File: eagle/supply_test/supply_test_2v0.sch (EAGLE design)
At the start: 27 parts, among them J21 AC_INSW, Q1 2N7002, U1 TPS62122

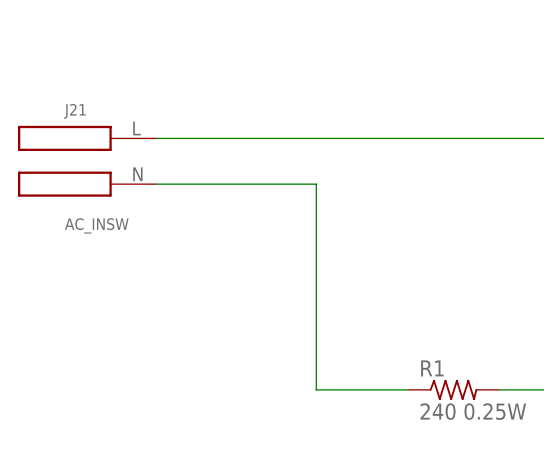
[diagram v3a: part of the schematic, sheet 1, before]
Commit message: finished updating shcematic
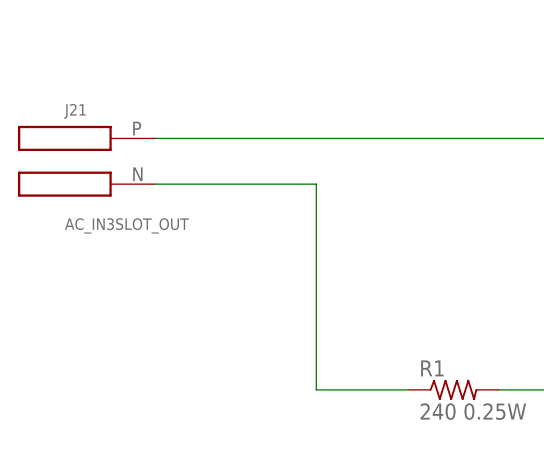
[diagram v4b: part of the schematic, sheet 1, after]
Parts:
- J21: value AC_INSW -> AC_IN3SLOT_OUT; device powerfilm:AC_INSW -> powerfilm:AC_IN3SLOT_OUT
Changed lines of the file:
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@@
 <grid distance="0.1" unitdist="inch" unit="inch" style="lines" multiple="1" display="no" altdistance="0.01" altunitdist="inch" altunit="inch"/>
 <layers>
-<layer number="1" name="Top" color="4" fill="1" visible="no" active="no"/>
-<layer number="2" name="Route2" color="1" fill="3" visible="no" active="no"/>
-<layer number="3" name="Route3" color="4" fill="3" visible="no" active="no"/>
-<layer number="4" name="Route4" color="1" fill="4" visible="no" active="no"/>
-<layer number="5" name="Route5" color="4" fill="4" visible="no" active="no"/>
-<layer number="6" name="Route6" color="1" fill="8" visible="no" active="no"/>
-<layer number="7" name="Route7" color="4" fill="8" visible="no" active="no"/>
-<layer number="8" name="Route8" color="1" fill="2" visible="no" active="no"/>
-<layer number="9" name="Route9" color="4" fill="2" visible="no" active="no"/>
-<layer number="10" name="Route10" color="1" fill="7" visible="no" active="no"/>
-<layer number="11" name="Route11" color="4" fill="7" visible="no" active="no"/>
-<layer number="12" name="Route12" color="1" fill="5" visible="no" active="no"/>
-<layer number="13" name="Route13" color="4" fill="5" visible="no" active="no"/>
-<layer number="14" name="Route14" color="1" fill="6" visible="no" active="no"/>
-<layer number="15" name="Route15" color="4" fill="6" visible="no" active="no"/>
-<layer number="16" name="Bottom" color="1" fill="1" visible="no" active="no"/>
-<layer number="17" name="Pads" color="2" fill="1" visible="no" active="no"/>
-<layer number="18" name="Vias" color="2" fill="1" visible="no" active="no"/>
-<layer number="19" name="Unrouted" color="6" fill="1" visible="no" active="no"/>
-<layer number="20" name="Dimension" color="15" fill="1" visible="no" active="no"/>
-<layer number="21" name="tPlace" color="7" fill="1" visible="no" active="no"/>
-<layer number="22" name="bPlace" color="7" fill="1" visible="no" active="no"/>
-<layer number="23" name="tOrigins" color="15" fill="1" visible="no" active="no"/>
-<layer number="24" name="bOrigins" color="15" fill="1" visible="no" active="no"/>
-<layer number="25" name="tNames" color="7" fill="1" visible="no" active="no"/>
-<layer number="26" name="bNames" color="7" fill="1" visible="no" active="no"/>
-<layer number="27" name="tValues" color="7" fill="1" visible="no" active="no"/>
-<layer number="28" name="bValues" color="7" fill="1" visible="no" active="no"/>
+<layer number="1" name="Top" color="4" fill="1" visible="yes" active="no"/>
+<layer number="2" name="Route2" color="1" fill="3" visible="yes" active="no"/>
+<layer number="3" name="Route3" color="4" fill="3" visible="yes" active="no"/>
+<layer number="4" name="Route4" color="1" fill="4" visible="yes" active="no"/>
+<layer number="5" name="Route5" color="4" fill="4" visible="yes" active="no"/>
+<layer number="6" name="Route6" color="1" fill="8" visible="yes" active="no"/>
+<layer number="7" name="Route7" color="4" fill="8" visible="yes" active="no"/>
+<layer number="8" name="Route8" color="1" fill="2" visible="yes" active="no"/>
+<layer number="9" name="Route9" color="4" fill="2" visible="yes" active="no"/>
+<layer number="10" name="Route10" color="1" fill="7" visible="yes" active="no"/>
+<layer number="11" name="Route11" color="4" fill="7" visible="yes" active="no"/>
+<layer number="12" name="Route12" color="1" fill="5" visible="yes" active="no"/>
+<layer number="13" name="Route13" color="4" fill="5" visible="yes" active="no"/>
+<layer number="14" name="Route14" color="1" fill="6" visible="yes" active="no"/>
+<layer number="15" name="Route15" color="4" fill="6" visible="yes" active="no"/>
+<layer number="16" name="Bottom" color="1" fill="1" visible="yes" active="no"/>
+<layer number="17" name="Pads" color="2" fill="1" visible="yes" active="no"/>
+<layer number="18" name="Vias" color="2" fill="1" visible="yes" active="no"/>
+<layer number="19" name="Unrouted" color="6" fill="1" visible="yes" active="no"/>
+<layer number="20" name="Dimension" color="15" fill="1" visible="yes" active="no"/>
+<layer number="21" name="tPlace" color="7" fill="1" visible="yes" active="no"/>
+<layer number="22" name="bPlace" color="7" fill="1" visible="yes" active="no"/>
+<layer number="23" name="tOrigins" color="15" fill="1" visible="yes" active="no"/>
+<layer number="24" name="bOrigins" color="15" fill="1" visible="yes" active="no"/>
+<layer number="25" name="tNames" color="7" fill="1" visible="yes" active="no"/>
+<layer number="26" name="bNames" color="7" fill="1" visible="yes" active="no"/>
+<layer number="27" name="tValues" color="7" fill="1" visible="yes" active="no"/>
+<layer number="28" name="bValues" color="7" fill="1" visible="yes" active="no"/>
 <layer number="29" name="tStop" color="7" fill="3" visible="no" active="no"/>
 <layer number="30" name="bStop" color="7" fill="6" visible="no" active="no"/>
@@
 <layer number="35" name="tGlue" color="7" fill="4" visible="no" active="no"/>
 <layer number="36" name="bGlue" color="7" fill="5" visible="no" active="no"/>
-<layer number="37" name="tTest" color="7" fill="1" visible="no" active="no"/>
-<layer number="38" name="bTest" color="7" fill="1" visible="no" active="no"/>
+<layer number="37" name="tTest" color="7" fill="1" visible="yes" active="no"/>
+<layer number="38" name="bTest" color="7" fill="1" visible="yes" active="no"/>
 <layer number="39" name="tKeepout" color="4" fill="11" visible="no" active="no"/>
 <layer number="40" name="bKeepout" color="1" fill="11" visible="no" active="no"/>
@@
 <layer number="44" name="Drills" color="7" fill="1" visible="no" active="no"/>
 <layer number="45" name="Holes" color="7" fill="1" visible="no" active="no"/>
-<layer number="46" name="Milling" color="3" fill="1" visible="no" active="no"/>
-<layer number="47" name="Measures" color="7" fill="1" visible="no" active="no"/>
-<layer number="48" name="Document" color="7" fill="1" visible="no" active="no"/>
-<layer number="49" name="Reference" color="7" fill="1" visible="no" active="no"/>
-<layer number="50" name="dxf" color="7" fill="1" visible="no" active="no"/>
-<layer number="51" name="tDocu" color="7" fill="1" visible="no" active="no"/>
-<layer number="52" name="bDocu" color="7" fill="1" visible="no" active="no"/>
-<layer number="53" name="tGND_GNDA" color="7" fill="9" visible="no" active="no"/>
-<layer number="54" name="bGND_GNDA" color="1" fill="9" visible="no" active="no"/>
-<layer number="56" name="wert" color="7" fill="1" visible="no" active="no"/>
+<layer number="46" name="Milling" color="3" fill="1" visible="yes" active="no"/>
+<layer number="47" name="Measures" color="7" fill="1" visible="yes" active="no"/>
+<layer number="48" name="Document" color="7" fill="1" visible="yes" active="no"/>
+<layer number="49" name="Reference" color="7" fill="1" visible="yes" active="no"/>
+<layer number="50" name="dxf" color="7" fill="1" visible="yes" active="no"/>
+<layer number="51" name="tDocu" color="7" fill="1" visible="yes" active="no"/>
+<layer number="52" name="bDocu" color="7" fill="1" visible="yes" active="no"/>
+<layer number="53" name="tGND_GNDA" color="7" fill="9" visible="yes" active="no"/>
+<layer number="54" name="bGND_GNDA" color="1" fill="9" visible="yes" active="no"/>
+<layer number="56" name="wert" color="7" fill="1" visible="yes" active="no"/>
 <layer number="91" name="Nets" color="2" fill="1" visible="yes" active="yes"/>
 <layer number="92" name="Busses" color="1" fill="1" visible="yes" active="yes"/>
@@
 <part name="GND1" library="supply1" deviceset="GND" device=""/>
 <part name="P+1" library="supply1" deviceset="VCC" device=""/>
-<part name="J21" library="powerfilm" deviceset="AC_IN" device="SW" value="AC_INSW">
+<part name="J21" library="powerfilm" deviceset="AC_IN" device="3SLOT_OUT" value="AC_IN3SLOT_OUT">
 <attribute name="DIGIKEY_2" value="AE9888-ND"/>
 </part>

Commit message: updated to film type
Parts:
- J21: value AC_IN3SLOT_OUT -> AC_INFILM; device powerfilm:AC_IN3SLOT_OUT -> powerfilm:AC_INFILM
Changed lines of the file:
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@@
 <part name="GND1" library="supply1" deviceset="GND" device=""/>
 <part name="P+1" library="supply1" deviceset="VCC" device=""/>
-<part name="J21" library="powerfilm" deviceset="AC_IN" device="3SLOT_OUT" value="AC_IN3SLOT_OUT">
+<part name="J21" library="powerfilm" deviceset="AC_IN" device="FILM" value="AC_INFILM">
 <attribute name="DIGIKEY_2" value="AE9888-ND"/>
 </part>

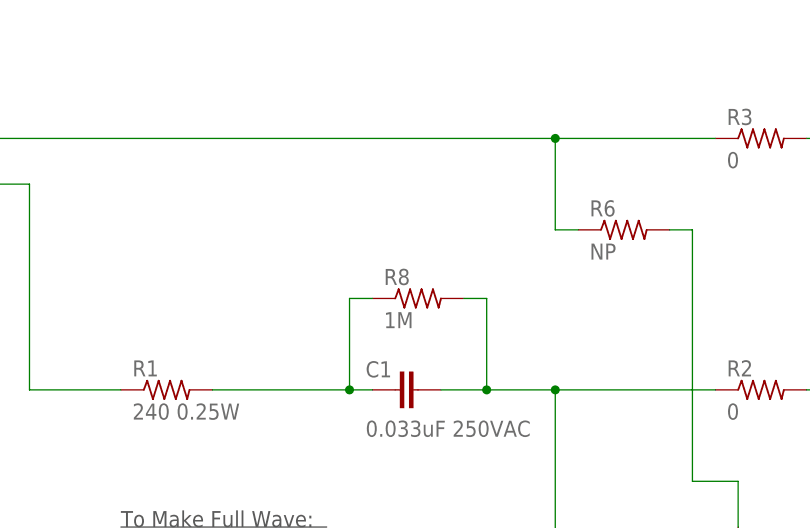
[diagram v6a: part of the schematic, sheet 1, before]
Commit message: re-arranged full wave and enable
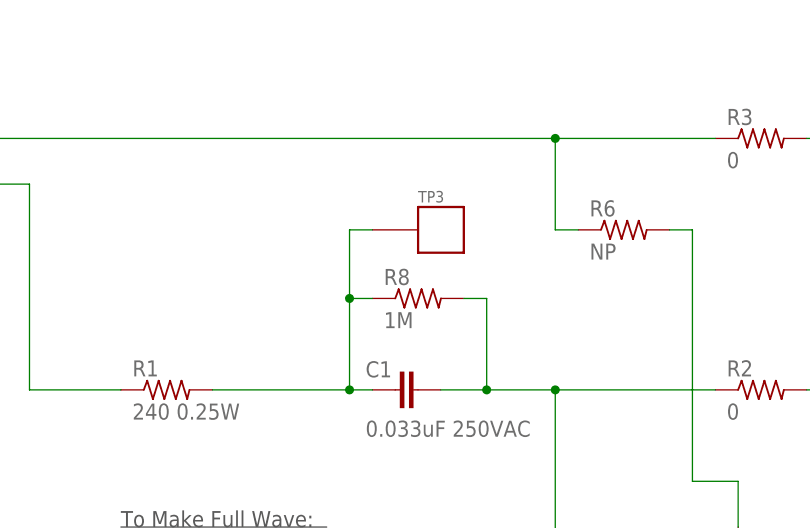
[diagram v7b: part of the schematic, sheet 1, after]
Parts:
- added TP3, TP4: TP_STD, skyspecs:TP_STD
- C7, C8: device rcl:C-EUC0603 -> rcl:C-EUC0402
- R10: device rcl:R-US_R0603 -> rcl:R-US_R0402
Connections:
- net +3V3: now also TP4.P$1
- net N$1: now also TP3.P$1
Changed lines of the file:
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@@
 <part name="GND4" library="supply1" deviceset="GND" device=""/>
 <part name="C4" library="rcl" deviceset="C-EU" device="C0603" value="22pF"/>
-<part name="R10" library="rcl" deviceset="R-US_" device="R0603" value="4.99k"/>
+<part name="R10" library="rcl" deviceset="R-US_" device="R0402" value="4.99k"/>
 <part name="Q1" library="nav" deviceset="2N7002" device=""/>
 <part name="GND5" library="supply1" deviceset="GND" device=""/>
@@
 <part name="+3V1" library="supply1" deviceset="+3V3" device=""/>
 <part name="P+2" library="supply1" deviceset="VCC" device=""/>
-<part name="C7" library="rcl" deviceset="C-EU" device="C0603" value="4.7uF"/>
-<part name="C8" library="rcl" deviceset="C-EU" device="C0603" value="0.1uF"/>
+<part name="C7" library="rcl" deviceset="C-EU" device="C0402" value="4.7uF"/>
+<part name="C8" library="rcl" deviceset="C-EU" device="C0402" value="0.1uF"/>
 <part name="C9" library="rcl" deviceset="C-EU" device="C0603" value="0.1uF"/>
 <part name="C10" library="rcl" deviceset="C-EU" device="C0603" value="4.7uF"/>
@@
 <part name="P+3" library="supply1" deviceset="VCC" device=""/>
 <part name="R6" library="rcl" deviceset="R-US_" device="R0603" value="NP"/>
+<part name="TP3" library="skyspecs" deviceset="TP" device="_STD">
+<attribute name="DIGIKEY" value="5000K-ND "/>
+</part>
+<part name="TP4" library="skyspecs" deviceset="TP" device="_STD"/>
 </parts>
 <sheets>
@@
 <instance part="P+3" gate="VCC" x="73.66" y="-25.4"/>
 <instance part="R6" gate="G$1" x="33.02" y="7.62"/>
+<instance part="TP3" gate="G$1" x="10.16" y="7.62">
+<attribute name="DIGIKEY" x="10.16" y="7.62" size="1.778" layer="96" display="off"/>
+</instance>
 </instances>
 <busses>
@@
 <wire x1="2.54" y1="0" x2="2.54" y2="-10.16" width="0.1524" layer="91"/>
 <junction x="2.54" y="-10.16"/>
+<pinref part="TP3" gate="G$1" pin="P$1"/>
+<wire x1="5.08" y1="7.62" x2="2.54" y2="7.62" width="0.1524" layer="91"/>
+<wire x1="2.54" y1="7.62" x2="2.54" y2="0" width="0.1524" layer="91"/>
+<junction x="2.54" y="0"/>
 </segment>
 </net>
@@
 <instance part="GND6" gate="1" x="-66.04" y="-30.48"/>
 <instance part="GND7" gate="1" x="63.5" y="-30.48"/>
+<instance part="TP4" gate="G$1" x="50.8" y="10.16"/>
 </instances>
 <busses>
@@
 <wire x1="53.34" y1="5.08" x2="53.34" y2="2.54" width="0.1524" layer="91"/>
 <junction x="53.34" y="5.08"/>
-</segment>
-</net>
+<pinref part="TP4" gate="G$1" pin="P$1"/>
+<wire x1="45.72" y1="10.16" x2="40.64" y2="10.16" width="0.1524" layer="91"/>
+<junction x="40.64" y="10.16"/>
+</segment>
+</net>
